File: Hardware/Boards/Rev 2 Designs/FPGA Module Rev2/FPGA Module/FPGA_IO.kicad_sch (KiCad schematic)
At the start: 55 parts, among them Q6 FDG1024NZ, Q7 FDG1024NZ, SW3 RST, U1 XCKU3P-FFVA676, U2 TXB0108DQSR, U3 Si511J200

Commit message: FPGA Module Rev 2 Layout Begun
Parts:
- removed C1, C2, C6, C7: 100nF, Capacitor_SMD:C_0201_0603Metric, symbol Device:C_Small
- removed R11, R12, R14, R15: 1K, Resistor_SMD:R_0201_0603Metric, symbol Device:R_US
- removed R13, R5: 100R, Resistor_SMD:R_0201_0603Metric, symbol Device:R_US
- removed R4: 0R, Resistor_SMD:R_0201_0603Metric, symbol Device:R_US
- removed TP10, TP9: Test Point, FPGA Module:Test Point 0.5mm No Silk, symbol Connector:TestPoint
- removed U2: TXB0108DQSR, Package_SON:USON-20_2x4mm_P0.4mm, symbol Logic_LevelTranslator:TXB0108DQSR
- added R3: 240R, Resistor_SMD:R_0201_0603Metric, symbol Device:R_US
- renumbered C44 to C1, C4 to C2, D4 to D1, D3 to D2, D2 to D3, D1 to D4, Q6 to Q1, Q7 to Q2, R16 to R10, R20 to R11, R21 to R12, R22 to R13, R23 to R14, R10 to R15, R24 to R16, R25 to R17, R26 to R18, R27 to R19, R28 to R20, R29 to R21, R30 to R22, R31 to R23, R3 to R4, R9 to R5, R8 to R6, R19 to R7, R18 to R8, R17 to R9, SW3 to SW1, TP14 to TP10, TP15 to TP11, TP16 to TP12, TP17 to TP13, TP18 to TP14, TP6 to TP5, TP7 to TP6, TP11 to TP7, TP12 to TP8, TP13 to TP9, U3 to U2
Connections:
- net FPGA_SPI_CS is gone; now on net D3_8: U1.R18 (IO_L19P_T3L_N0_DBC_AD9P_64)
- net FPGA_SPI_MISO is gone; now on net D3_11: U1.R21 (IO_L20N_T3L_N3_AD1N_64)
- net FPGA_SPI_MOSI is gone; now on net D3_10: U1.P21 (IO_L20P_T3L_N2_AD1P_64)
- net FPGA_SPI_SCK is gone; now on net D3_9: U1.T18 (IO_L19N_T3L_N1_DBC_AD9N_64)
- net HDMI_CEC is gone; now on net RST2: U1.AB22 (IO_L3N_T0L_N5_AD15N_64)
- net HDMI_CLK_SEL is gone; now on net RWDS2_0: U1.U25 (IO_T1U_N12_64)
- net HDMI_EQ_SEL is gone; now on net D2_4: U1.Y23 (IO_L5P_T0U_N8_AD14P_64)
- net HDMI_HPD_SRC is gone; now on net CK2_N: U1.AA25 (IO_L4P_T0U_N6_DBC_AD7P_64)
- net HDMI_I2C_EN is gone; now on net D2_14: U1.V24 (IO_L11N_T1U_N9_GC_64)
- net HDMI_LVCLK_N is gone; now on net IO1: U1.F8 (IO_L20N_T3L_N3_AD1N_66)
- net HDMI_LVCLK_P is gone; now on net IO6: U1.F9 (IO_L20P_T3L_N2_AD1P_66)
- net HDMI_OE is gone; now on net CS2: U1.AA22 (IO_L3P_T0L_N4_AD15P_64)
- net HDMI_SCL_SRC is gone; now on net D2_7: U1.AC24 (IO_L6N_T0U_N11_AD6N_64)
- net HDMI_SDA_SRC is gone; now on net D2_6: U1.AC23 (IO_L6P_T0U_N10_AD6P_64)
- net HDMI_SDA_SRC_EN is gone; now on net D2_3: U1.AC26 (IO_L2N_T0L_N3_64)
- net HDMI_SEL is gone; now on net D2_5: U1.AA23 (IO_L5N_T0U_N9_AD14N_64)
- net HDMI_SLEW_CTL is gone; now on net D2_2: U1.AB26 (IO_L2P_T0L_N2_64)
- net MBUS_D14 is gone; now on net FPGA_I2C_SCL: U1.AE16 (IO_L1P_AD11P_84)
- net MEMCLK_N is gone; now on net FIFO_BE0: U1.F12 (IO_L11N_T1U_N9_GC_66)
- net MEMCLK_P is gone; now on net FIFO_D0: U1.G12 (IO_L11P_T1U_N8_GC_66)
- net SYSCLK1_N is gone; now on net CK3_P: U1.T24 (IO_L13N_T2L_N1_GC_QBC_64)
- net SYSCLK1_P is gone; now on net CK3_N: U1.T23 (IO_L13P_T2L_N0_GC_QBC_64)
- net TPD5_EN is gone; now on net CK2_P: U1.AB25 (IO_L4N_T0U_N7_DBC_AD7N_64)
- net CAM_LED_EN: now also U1.AB14 (IO_L9N_AD3N_84); no longer U1.AF10 (IO_L4N_AD12N_85)
- net CAM_PWR_EN: now also U1.AA14 (IO_L9P_AD3P_84); no longer U1.AE11 (IO_L2N_AD14N_85)
- net CK2_N: no longer U1.AF22 (IO_L19N_T3L_N1_DBC_AD9N_D11_65)
- net CK2_P: no longer U1.AE22 (IO_L19P_T3L_N0_DBC_AD9P_D10_65)
- net CK3_N: no longer U1.AA20 (IO_L13N_T2L_N1_GC_QBC_A07_D23_65)
- net CK3_P: no longer U1.AA19 (IO_L13P_T2L_N0_GC_QBC_A06_D22_65)
- net CS2: no longer U1.AE26 (IO_L22N_T3U_N7_DBC_AD0N_D05_65)
- net CS3: now also U1.Y26 (IO_L9N_T1L_N5_AD12N_64); no longer U1.AE21 (IO_L16N_T2U_N7_QBC_AD3N_A01_D17_65)
- net D2_0: now also U1.AA24 (IO_L1P_T0L_N0_DBC_64); no longer U1.AD25 (IO_L24N_T3U_N11_DOUT_CSO_B_65)
- net D2_1: now also U1.AB24 (IO_L1N_T0L_N1_DBC_64); no longer U1.AD24 (IO_L24P_T3U_N10_EMCCLK_65)
- net D2_10: now also U1.W26 (IO_L8N_T1L_N3_AD5N_64); no longer U1.AC21 (IO_L17N_T2U_N9_AD10N_D15_65)
- net D2_11: now also U1.Y25 (IO_L9P_T1L_N4_AD12P_64); no longer U1.AB21 (IO_L17P_T2U_N8_AD10P_D14_65)
- net D2_12: now also U1.V26 (IO_L10N_T1U_N7_QBC_AD4N_64); no longer U1.AD19 (IO_L15N_T2L_N5_AD11N_A03_D19_65)
- net D2_13: now also U1.U24 (IO_L11P_T1U_N8_GC_64); no longer U1.AC19 (IO_L15P_T2L_N4_AD11P_A02_D18_65)
- net D2_14: no longer U1.AB20 (IO_L14N_T2L_N3_GC_A05_D21_65)
- net D2_15: now also U1.V22 (IO_L12P_T1U_N10_GC_64); no longer U1.AB19 (IO_L14P_T2L_N2_GC_A04_D20_65)
- net D2_2: no longer U1.AE23 (IO_L23N_T3U_N9_PERSTN1_I2C_SDA_65)
- net D2_3: no longer U1.AD23 (IO_L23P_T3U_N8_I2C_SCLK_65)
- net D2_4: no longer U1.AF24 (IO_L21N_T3L_N5_AD8N_D07_65)
- net D2_5: no longer U1.AF23 (IO_L21P_T3L_N4_AD8P_D06_65)
- net D2_6: no longer U1.AF25 (IO_L20N_T3L_N3_AD1N_D09_65)
- net D2_7: no longer U1.AE25 (IO_L20P_T3L_N2_AD1P_D08_65)
- net D2_8: now also U1.W24 (IO_L7N_T1L_N1_QBC_AD13N_64); no longer U1.AD21 (IO_L18N_T2U_N11_AD2N_D13_65)
- net D2_9: now also U1.W25 (IO_L8P_T1L_N2_AD5P_64); no longer U1.AD20 (IO_L18P_T2U_N10_AD2P_D12_65)
- net D3_0: now also U1.R22 (IO_L16P_T2U_N6_QBC_AD3P_64); no longer U1.AB17 (IO_L2P_T0L_N2_FOE_B_65)
- net D3_1: now also U1.R23 (IO_L16N_T2U_N7_QBC_AD3N_64); no longer U1.AC17 (IO_L2N_T0L_N3_FWE_FCS2_B_65)
- net D3_10: no longer U1.W18 (IO_L9P_T1L_N4_AD12P_A14_D30_65)
- net D3_11: no longer U1.W19 (IO_L9N_T1L_N5_AD12N_A15_D31_65)
- net D3_12: now also U1.P18 (IO_L21P_T3L_N4_AD8P_64); no longer U1.Y17 (IO_L11P_T1U_N8_GC_A10_D26_65)
- net D3_13: now also U1.P19 (IO_L21N_T3L_N5_AD8N_64); no longer U1.Y18 (IO_L11N_T1U_N9_GC_A11_D27_65)
- net D3_14: now also U1.T22 (IO_L14P_T2L_N2_GC_64); no longer U1.Y20 (IO_L12N_T1U_N11_GC_A09_D25_65)
- net D3_15: now also U1.U22 (IO_L14N_T2L_N3_GC_64); no longer U1.W20 (IO_L12P_T1U_N10_GC_A08_D24_65)
- net D3_2: now also U1.P23 (IO_L17P_T2U_N8_AD10P_64); no longer U1.AE17 (IO_L3P_T0L_N4_AD15P_A26_65)
- net D3_3: now also U1.P24 (IO_L17N_T2U_N9_AD10N_64); no longer U1.AE18 (IO_L3N_T0L_N5_AD15N_A27_65)
- net D3_4: now also U1.P25 (IO_L18P_T2U_N10_AD2P_64); no longer U1.AC18 (IO_L5P_T0U_N8_AD14P_A22_65)
- net D3_5: now also U1.R25 (IO_L18N_T2U_N11_AD2N_64); no longer U1.AD18 (IO_L5N_T0U_N9_AD14N_A23_65)
- net D3_6: now also U1.T25 (IO_T2U_N12_64); no longer U1.AF17 (IO_L6P_T0U_N10_AD6P_A20_65)
- net D3_7: now also U1.V21 (IO_T3U_N12_64); no longer U1.AF18 (IO_L6N_T0U_N11_AD6N_A21_65)
- net D3_8: no longer U1.W21 (IO_L8P_T1L_N2_AD5P_A16_65)
- net D3_9: no longer U1.Y21 (IO_L8N_T1L_N3_AD5N_A17_65)
- net FIFO_BE0: no longer U1.W13 (IO_L10N_AD2N_84)
- net FIFO_BE1: now also U1.E13 (IO_L12P_T1U_N10_GC_66); no longer U1.AA14 (IO_L9P_AD3P_84)
- net FIFO_CLK: now also U1.E10 (IO_L13P_T2L_N0_GC_QBC_66); no longer U1.AA15 (IO_L7P_HDGC_AD5P_84)
- net FIFO_D0: no longer U1.W9 (IO_L11P_AD9P_85)
- net FIFO_D1: now also U1.F13 (IO_L10N_T1U_N7_QBC_AD4N_66); no longer U1.AA9 (IO_L7N_HDGC_85)
- net FIFO_D10: now also U1.D15 (IO_T0U_N12_VRP_66); no longer U1.V11 (IO_L10N_AD10N_85)
- net FIFO_D11: now also U1.A12 (IO_L6N_T0U_N11_AD6N_66); no longer U1.Y11 (IO_L8P_HDGC_85)
- net FIFO_D12: now also U1.A13 (IO_L6P_T0U_N10_AD6P_66); no longer U1.AA10 (IO_L7P_HDGC_85)
- net FIFO_D13: now also U1.B12 (IO_L5N_T0U_N9_AD14N_66); no longer U1.AB10 (IO_L6P_HDGC_85)
- net FIFO_D14: now also U1.C12 (IO_L5P_T0U_N8_AD14P_66); no longer U1.W15 (IO_L8P_HDGC_AD4P_84)
- net FIFO_D15: now also U1.A14 (IO_L4N_T0U_N7_DBC_AD7N_66); no longer U1.Y15 (IO_L8N_HDGC_AD4N_84)
- net FIFO_D2: now also U1.F14 (IO_L10P_T1U_N6_QBC_AD4P_66); no longer U1.Y10 (IO_L8N_HDGC_85)
- net FIFO_D3: now also U1.H13 (IO_L9N_T1L_N5_AD12N_66); no longer U1.W11 (IO_L12P_AD8P_85)
- net FIFO_D4: now also U1.J13 (IO_L9P_T1L_N4_AD12P_66); no longer U1.V12 (IO_L10P_AD10P_85)
- net FIFO_D5: now also U1.F15 (IO_L8N_T1L_N3_AD5N_66); no longer U1.AB9 (IO_L6N_HDGC_85)
- net FIFO_D6: now also U1.G15 (IO_L8P_T1L_N2_AD5P_66); no longer U1.AC12 (IO_L1P_AD15P_85)
- net FIFO_D7: now also U1.G14 (IO_L7N_T1L_N1_QBC_AD13N_66); no longer U1.W14 (IO_L10P_AD2P_84)
- net FIFO_D8: now also U1.H14 (IO_L7P_T1L_N0_QBC_AD13P_66); no longer U1.AA8 (IO_L9N_AD11N_85)
- net FIFO_D9: now also U1.E15 (IO_T1U_N12_66); no longer U1.W10 (IO_L12N_AD8N_85)
- net FPGA_I2C_SCL: no longer U1.AC11 (IO_L1N_AD15N_85)
- net FPGA_I2C_SDA: now also U1.AF15 (IO_L1N_AD11N_84); no longer U1.AD11 (IO_L2P_AD14P_85)
- net FT600_OE: now also U1.B15 (IO_L2P_T0L_N2_66); no longer U1.AC9 (IO_L3P_AD13P_85)
- net FT600_RD: now also U1.A15 (IO_L2N_T0L_N3_66); no longer U1.Y8 (IO_L9P_AD11P_85)
- net FT600_RST: now also U1.C14 (IO_L1N_T0L_N1_DBC_66); no longer U1.AD8 (IO_L5N_HDGC_85)
- net FT600_RXE: now also U1.C13 (IO_L3N_T0L_N5_AD15N_66); no longer U1.AD9 (IO_L3N_AD13N_85)
- net FT600_TXE: now also U1.B14 (IO_L4P_T0U_N6_DBC_AD7P_66); no longer U1.AE10 (IO_L4P_AD12P_85)
- net FT600_WAKEUP: now also U1.D14 (IO_L1P_T0L_N0_DBC_66); no longer U1.AC8 (IO_L5P_HDGC_85)
- net FT600_WR: now also U1.D13 (IO_L3P_T0L_N4_AD15P_66); no longer U1.W8 (IO_L11N_AD9N_85)
- net GND: now also U1.A3 (MGTYRXN3_227), U1.A4 (MGTYRXP3_227), U1.AB1 (MGTYRXN3_224), U1.AB2 (MGTYRXP3_224), U1.AD1 (MGTYRXN2_224), U1.AD2 (MGTYRXP2_224), U1.AE3 (MGTYRXN1_224), U1.AE4 (MGTYRXP1_224), U1.AF1 (MGTYRXN0_224), U1.AF2 (MGTYRXP0_224), U1.AF7 (MGTRREF_R), U1.AF8 (MGTAVTTRCAL_R)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
- net IO0: now also U1.J9 (IO_L21N_T3L_N5_AD8N_66); no longer U1.P23 (IO_L17P_T2U_N8_AD10P_64)
- net IO1: no longer U1.P25 (IO_L18P_T2U_N10_AD2P_64)
- net IO2: now also U1.H9 (IO_L19P_T3L_N0_DBC_AD9P_66); no longer U1.V21 (IO_T3U_N12_64)
- net IO3: now also U1.H8 (IO_L19N_T3L_N1_DBC_AD9N_66); no longer U1.T25 (IO_T2U_N12_64)
- net IO4: now also U1.G11 (IO_L22P_T3U_N6_DBC_AD0P_66); no longer U1.R23 (IO_L16N_T2U_N7_QBC_AD3N_64)
- net IO5: now also U1.F10 (IO_L22N_T3U_N7_DBC_AD0N_66); no longer U1.R22 (IO_L16P_T2U_N6_QBC_AD3P_64)
- net IO6: no longer U1.R25 (IO_L18N_T2U_N11_AD2N_64)
- net IO7: now also U1.J10 (IO_L21P_T3L_N4_AD8P_66); no longer U1.P24 (IO_L17N_T2U_N9_AD10N_64)
- net LED0: now also U1.J11 (IO_L23P_T3U_N8_66); no longer U1.V26 (IO_L10N_T1U_N7_QBC_AD4N_64)
- net LED1: now also U1.H11 (IO_L23N_T3U_N9_66); no longer U1.U26 (IO_L10P_T1U_N6_QBC_AD4P_64)
- net LED2: now also U1.G10 (IO_L24P_T3U_N10_66); no longer U1.Y26 (IO_L9N_T1L_N5_AD12N_64)
- net LED3: now also U1.G9 (IO_L24N_T3U_N11_66); no longer U1.W26 (IO_L8N_T1L_N3_AD5N_64)
- net MBUS_D0: now also U1.E11 (IO_L14P_T2L_N2_GC_66); no longer U1.AD13 (IO_L6N_HDGC_AD6N_84)
- net MBUS_D1: now also U1.D11 (IO_L14N_T2L_N3_GC_66); no longer U1.AD14 (IO_L6P_HDGC_AD6P_84)
- net MBUS_D10: now also U1.D9 (IO_T2U_N12_66); no longer U1.AF14 (IO_L2P_AD10P_84)
- net MBUS_D11: now also U1.H12 (IO_T3U_N12_66); no longer U1.AF15 (IO_L1N_AD11N_84)
- net MBUS_D2: now also U1.C9 (IO_L15P_T2L_N4_AD11P_66); no longer U1.AD15 (IO_L3P_AD9P_84)
- net MBUS_D3: now also U1.C8 (IO_L15N_T2L_N5_AD11N_66); no longer U1.AC13 (IO_L5N_HDGC_AD7N_84)
- net MBUS_D4: now also U1.C11 (IO_L16P_T2U_N6_QBC_AD3P_66); no longer U1.AC14 (IO_L5P_HDGC_AD7P_84)
- net MBUS_D5: now also U1.B11 (IO_L16N_T2U_N7_QBC_AD3N_66); no longer U1.AB14 (IO_L9N_AD3N_84)
- net MBUS_D6: now also U1.E8 (IO_L17P_T2U_N8_AD10P_66); no longer U1.AB15 (IO_L7N_HDGC_AD5N_84)
- net MBUS_D7: now also U1.D8 (IO_L17N_T2U_N9_AD10N_66); no longer U1.AA13 (IO_L11P_AD1P_84)
- net MBUS_D8: now also U1.B10 (IO_L18P_T2U_N10_AD2P_66); no longer U1.AF12 (IO_L4N_AD8N_84)
- net MBUS_D9: now also U1.A10 (IO_L18N_T2U_N11_AD2N_66); no longer U1.AF13 (IO_L2N_AD10N_84)
- net MIPI_CLK_N: now also U1.AA20 (IO_L13N_T2L_N1_GC_QBC_A07_D23_65); no longer U1.D10 (IO_L13N_T2L_N1_GC_QBC_66)
- net MIPI_CLK_P: now also U1.AA19 (IO_L13P_T2L_N0_GC_QBC_A06_D22_65); no longer U1.E10 (IO_L13P_T2L_N0_GC_QBC_66)
- net MIPI_D0_N: now also U1.AB20 (IO_L14N_T2L_N3_GC_A05_D21_65); no longer U1.D11 (IO_L14N_T2L_N3_GC_66)
- net MIPI_D0_P: now also U1.AB19 (IO_L14P_T2L_N2_GC_A04_D20_65); no longer U1.E11 (IO_L14P_T2L_N2_GC_66)
- net MIPI_D1_N: now also U1.AD19 (IO_L15N_T2L_N5_AD11N_A03_D19_65); no longer U1.C8 (IO_L15N_T2L_N5_AD11N_66)
- net MIPI_D1_P: now also U1.AC19 (IO_L15P_T2L_N4_AD11P_A02_D18_65); no longer U1.C9 (IO_L15P_T2L_N4_AD11P_66)
- net MIPI_D2_N: now also U1.AD21 (IO_L18N_T2U_N11_AD2N_D13_65); no longer U1.A10 (IO_L18N_T2U_N11_AD2N_66)
- net MIPI_D2_P: now also U1.AD20 (IO_L18P_T2U_N10_AD2P_D12_65); no longer U1.B10 (IO_L18P_T2U_N10_AD2P_66)
- net MIPI_D3_N: now also U1.AC21 (IO_L17N_T2U_N9_AD10N_D15_65); no longer U1.D8 (IO_L17N_T2U_N9_AD10N_66)
- net MIPI_D3_P: now also U1.AB21 (IO_L17P_T2U_N8_AD10P_D14_65); no longer U1.E8 (IO_L17P_T2U_N8_AD10P_66)
- net RST2: no longer U1.AD26 (IO_L22P_T3U_N6_DBC_AD0P_D04_65)
- net RST3: now also U1.U26 (IO_L10P_T1U_N6_QBC_AD4P_64); no longer U1.AE20 (IO_L16P_T2U_N6_QBC_AD3P_A00_D16_65)
- net RWDS2_0: no longer U1.AC22 (IO_T3U_N12_PERSTN0_65)
- net RWDS2_1: now also U1.W23 (IO_L7P_T1L_N0_QBC_AD13P_64); no longer U1.AA18 (IO_T2U_N12_CSI_ADV_B_65)
- net RWDS3_0: now also U1.P26 (IO_L15P_T2L_N4_AD11P_64); no longer U1.AC16 (IO_L1P_T0L_N0_DBC_RS0_65)
- net RWDS3_1: now also U1.R26 (IO_L15N_T2L_N5_AD11N_64); no longer U1.AD16 (IO_L1N_T0L_N1_DBC_RS1_65)
- net SYS_SPI_CS: now also U1.W13 (IO_L10N_AD2N_84)
- net SYS_SPI_MISO: now also U1.W14 (IO_L10P_AD2P_84)
- net SYS_SPI_MOSI: now also U1.AA12 (IO_L11N_AD1N_84)
- net SYS_SPI_SCK: now also U1.AA13 (IO_L11P_AD1P_84)
- net UART_RX: now also U1.AB11 (IO_L12N_AD0N_84); no longer U1.P26 (IO_L15P_T2L_N4_AD11P_64)
- net UART_TX: now also U1.AB12 (IO_L12P_AD0P_84); no longer U1.R26 (IO_L15N_T2L_N5_AD11N_64)
- net at R15.2: now also U1.AF18 (IO_L6N_T0U_N11_AD6N_A21_65); no longer U1.D15 (IO_T0U_N12_VRP_66)
- net GTCLK0_N: no longer names the net of U1.M5 (MGTREFCLK0N_226)
- net GTCLK0_P: no longer names the net of U1.M6 (MGTREFCLK0P_226)
- net GTCLK1_N: no longer names the net of U1.K5 (MGTREFCLK1N_226)
- net GTCLK1_P: no longer names the net of U1.K6 (MGTREFCLK1P_226)
- net HDMI_D0_N: no longer names the net of U1.J3 (MGTYTXN2_226)
- net HDMI_D0_P: no longer names the net of U1.J4 (MGTYTXP2_226)
- net HDMI_D1_N: no longer names the net of U1.L3 (MGTYTXN1_226)
- net HDMI_D1_P: no longer names the net of U1.L4 (MGTYTXP1_226)
- net HDMI_D2_N: no longer names the net of U1.N3 (MGTYTXN0_226)
- net HDMI_D2_P: no longer names the net of U1.N4 (MGTYTXP0_226)
- net HDMI_GTCLK_N: no longer names the net of U1.G3 (MGTYTXN3_226)
- net HDMI_GTCLK_P: no longer names the net of U1.G4 (MGTYTXP3_226)
- net HDMI_PRE_SEL: no longer names the net of U1.Y22 (IO_T0U_N12_VRP_64)
- net HDMI_PRE_SEL: now also R3.2
- net MBUS_D12 renamed HDMI_SD0_DL0
- net MBUS_D13 renamed HDMI_SD1_DR1
- new net HDMI_DB0: U1.Y8 (IO_L9P_AD11P_85)
- new net HDMI_DB1: U1.AA8 (IO_L9N_AD11N_85)
- new net HDMI_DB2: U1.V12 (IO_L10P_AD10P_85)
- new net HDMI_DB3: U1.V11 (IO_L10N_AD10N_85)
- new net HDMI_DB4: U1.W9 (IO_L11P_AD9P_85)
- new net HDMI_DB5: U1.W8 (IO_L11N_AD9N_85)
- new net HDMI_DB6: U1.W11 (IO_L12P_AD8P_85)
- new net HDMI_DB7: U1.W10 (IO_L12N_AD8N_85)
- new net HDMI_DE: U1.Y15 (IO_L8N_HDGC_AD4N_84)
- new net HDMI_DG0: U1.AC8 (IO_L5P_HDGC_85)
- new net HDMI_DG1: U1.AD8 (IO_L5N_HDGC_85)
- new net HDMI_DG2: U1.AB10 (IO_L6P_HDGC_85)
- new net HDMI_DG3: U1.AB9 (IO_L6N_HDGC_85)
- new net HDMI_DG4: U1.AA10 (IO_L7P_HDGC_85)
- new net HDMI_DG5: U1.AA9 (IO_L7N_HDGC_85)
- new net HDMI_DG6: U1.Y11 (IO_L8P_HDGC_85)
- new net HDMI_DG7: U1.Y10 (IO_L8N_HDGC_85)
- new net HDMI_DR0: U1.AC12 (IO_L1P_AD15P_85)
- new net HDMI_DR1: U1.AC11 (IO_L1N_AD15N_85)
- new net HDMI_DR2: U1.AD11 (IO_L2P_AD14P_85)
- new net HDMI_DR3: U1.AE11 (IO_L2N_AD14N_85)
- new net HDMI_DR4: U1.AC9 (IO_L3P_AD13P_85)
- new net HDMI_DR5: U1.AD9 (IO_L3N_AD13N_85)
- new net HDMI_DR6: U1.AE10 (IO_L4P_AD12P_85)
- new net HDMI_DR7: U1.AF10 (IO_L4N_AD12N_85)
- new net HDMI_HSYNC: U1.W15 (IO_L8P_HDGC_AD4P_84)
- new net HDMI_IDCLK: U1.AA15 (IO_L7P_HDGC_AD5P_84)
- new net HDMI_INT: U1.AD14 (IO_L6P_HDGC_AD6P_84)
- new net HDMI_MCLK: U1.AC13 (IO_L5N_HDGC_AD7N_84)
- new net HDMI_RST: U1.AD13 (IO_L6N_HDGC_AD6N_84)
- new net HDMI_SCK: U1.AC14 (IO_L5P_HDGC_AD7P_84)
- new net HDMI_SD2_DL1: U1.AD15 (IO_L3P_AD9P_84)
- new net HDMI_SD3_DR2: U1.AF13 (IO_L2N_AD10N_84)
- new net HDMI_SPDIF: U1.AF14 (IO_L2P_AD10P_84)
- new net HDMI_VSYNC: U1.AB15 (IO_L7N_HDGC_AD5N_84)
- new net HDMI_WS_DR0: U1.AF12 (IO_L4N_AD8N_84)
- no-connect marks 113 -> 101
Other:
- note removed: "HDMI"
- moved on the sheet: D1, D2, D3, D4, Q1A, Q1B, Q2A, Q2B, R10, R11, R12, R13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

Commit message: Completed B2B and HyperRam routing
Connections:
- net CK0_N: now also U1.A25 (IO_L1N_T0L_N1_DBC_67); no longer U1.A18 (IO_L15N_T2L_N5_AD11N_67)
- net CK0_P: now also U1.A24 (IO_L1P_T0L_N0_DBC_67); no longer U1.A17 (IO_L15P_T2L_N4_AD11P_67)
- net CK1_N: now also U1.C18 (IO_L14N_T2L_N3_GC_67); no longer U1.A23 (IO_L7N_T1L_N1_QBC_AD13N_67)
- net CK1_P: now also U1.D18 (IO_L14P_T2L_N2_GC_67); no longer U1.A22 (IO_L7P_T1L_N0_QBC_AD13P_67)
- net CK2_N: now also U1.P24 (IO_L17N_T2U_N9_AD10N_64); no longer U1.AA25 (IO_L4P_T0U_N6_DBC_AD7P_64)
- net CK2_P: now also U1.P23 (IO_L17P_T2U_N8_AD10P_64); no longer U1.AB25 (IO_L4N_T0U_N7_DBC_AD7N_64)
- net CK3_N: now also U1.V26 (IO_L10N_T1U_N7_QBC_AD4N_64); no longer U1.T23 (IO_L13P_T2L_N0_GC_QBC_64)
- net CK3_P: now also U1.U26 (IO_L10P_T1U_N6_QBC_AD4P_64); no longer U1.T24 (IO_L13N_T2L_N1_GC_QBC_64)
- net CS0: now also U1.A23 (IO_L7N_T1L_N1_QBC_AD13N_67); no longer U1.B17 (IO_L18N_T2U_N11_AD2N_67)
- net CS1: now also U1.C17 (IO_L18P_T2U_N10_AD2P_67); no longer U1.A20 (IO_L8N_T1L_N3_AD5N_67)
- net CS2: now also U1.R22 (IO_L16P_T2U_N6_QBC_AD3P_64); no longer U1.AA22 (IO_L3P_T0L_N4_AD15P_64)
- net CS3: now also U1.U25 (IO_T1U_N12_64); no longer U1.Y26 (IO_L9N_T1L_N5_AD12N_64)
- net D0_0: now also U1.B21 (IO_L9P_T1L_N4_AD12P_67); no longer U1.E17 (IO_L23P_T3U_N8_67)
- net D0_1: now also U1.C21 (IO_L10P_T1U_N6_QBC_AD4P_67); no longer U1.G17 (IO_L20P_T3L_N2_AD1P_67)
- net D0_10: now also U1.B26 (IO_L6N_T0U_N11_AD6N_67); no longer U1.F20 (IO_L19N_T3L_N1_DBC_AD9N_67)
- net D0_11: now also U1.C22 (IO_L10N_T1U_N7_QBC_AD4N_67); no longer U1.C16 (IO_L17P_T2U_N8_AD10P_67)
- net D0_12: now also U1.D25 (IO_L2P_T0L_N2_67); no longer U1.D19 (IO_L13P_T2L_N0_GC_QBC_67)
- net D0_13: now also U1.C23 (IO_L4N_T0U_N7_DBC_AD7N_67); no longer U1.B19 (IO_L16P_T2U_N6_QBC_AD3P_67)
- net D0_14: now also U1.D26 (IO_L2N_T0L_N3_67); no longer U1.F19 (IO_L21N_T3L_N5_AD8N_67)
- net D0_15: now also U1.C24 (IO_L5N_T0U_N9_AD14N_67); no longer U1.A19 (IO_L16N_T2U_N7_QBC_AD3N_67)
- net D0_2: now also U1.A20 (IO_L8N_T1L_N3_AD5N_67); no longer U1.G19 (IO_L19P_T3L_N0_DBC_AD9P_67)
- net D0_3: now also U1.B25 (IO_L3N_T0L_N5_AD15N_67); no longer U1.F18 (IO_L21P_T3L_N4_AD8P_67)
- net D0_4: now also U1.A19 (IO_L16N_T2U_N7_QBC_AD3N_67); no longer U1.B16 (IO_L17N_T2U_N9_AD10N_67)
- net D0_5: now also U1.B24 (IO_L3P_T0L_N4_AD15P_67); no longer U1.E18 (IO_L23N_T3U_N9_67)
- net D0_6: now also U1.D23 (IO_L4P_T0U_N6_DBC_AD7P_67); no longer U1.E16 (IO_T3U_N12_67)
- net D0_7: now also U1.D21 (IO_L12N_T1U_N11_GC_67); no longer U1.D16 (IO_T2U_N12_67)
- net D0_8: now also U1.D24 (IO_L5P_T0U_N8_AD14P_67); no longer U1.D18 (IO_L14P_T2L_N2_GC_67)
- net D0_9: now also U1.B22 (IO_L9N_T1L_N5_AD12N_67); no longer U1.C18 (IO_L14N_T2L_N3_GC_67)
- net D1_0: now also U1.D20 (IO_L12P_T1U_N10_GC_67); no longer U1.B21 (IO_L9P_T1L_N4_AD12P_67)
- net D1_1: now also U1.E21 (IO_L11N_T1U_N9_GC_67); no longer U1.B22 (IO_L9N_T1L_N5_AD12N_67)
- net D1_10: now also U1.H18 (IO_L24N_T3U_N11_67); no longer U1.D26 (IO_L2N_T0L_N3_67)
- net D1_11: now also U1.E17 (IO_L23P_T3U_N8_67); no longer U1.E21 (IO_L11N_T1U_N9_GC_67)
- net D1_12: now also U1.G17 (IO_L20P_T3L_N2_AD1P_67); no longer U1.C26 (IO_L6P_T0U_N10_AD6P_67)
- net D1_13: now also U1.E16 (IO_T3U_N12_67); no longer U1.A24 (IO_L1P_T0L_N0_DBC_67)
- net D1_14: now also U1.G19 (IO_L19P_T3L_N0_DBC_AD9P_67); no longer U1.C24 (IO_L5N_T0U_N9_AD14N_67)
- net D1_15: now also U1.E18 (IO_L23N_T3U_N9_67); no longer U1.A25 (IO_L1N_T0L_N1_DBC_67)
- net D1_2: now also U1.A17 (IO_L15P_T2L_N4_AD11P_67); no longer U1.D25 (IO_L2P_T0L_N2_67)
- net D1_3: now also U1.F19 (IO_L21N_T3L_N5_AD8N_67); no longer U1.C21 (IO_L10P_T1U_N6_QBC_AD4P_67)
- net D1_4: now also U1.A18 (IO_L15N_T2L_N5_AD11N_67); no longer U1.D24 (IO_L5P_T0U_N8_AD14P_67)
- net D1_5: now also U1.F20 (IO_L19N_T3L_N1_DBC_AD9N_67); no longer U1.C23 (IO_L4N_T0U_N7_DBC_AD7N_67)
- net D1_6: now also U1.E20 (IO_L11P_T1U_N8_GC_67); no longer U1.C22 (IO_L10N_T1U_N7_QBC_AD4N_67)
- net D1_7: now also U1.C16 (IO_L17P_T2U_N8_AD10P_67); no longer U1.E20 (IO_L11P_T1U_N8_GC_67)
- net D1_8: now also U1.F17 (IO_L20N_T3L_N3_AD1N_67); no longer U1.B25 (IO_L3N_T0L_N5_AD15N_67)
- net D1_9: now also U1.D16 (IO_T2U_N12_67); no longer U1.B24 (IO_L3P_T0L_N4_AD15P_67)
- net D2_0: now also U1.T20 (IO_L22N_T3U_N7_DBC_AD0N_64); no longer U1.AA24 (IO_L1P_T0L_N0_DBC_64)
- net D2_1: now also U1.R20 (IO_L23N_T3U_N9_64); no longer U1.AB24 (IO_L1N_T0L_N1_DBC_64)
- net D2_10: now also U1.V23 (IO_L12N_T1U_N11_GC_64); no longer U1.W26 (IO_L8N_T1L_N3_AD5N_64)
- net D2_11: now also U1.U21 (IO_L24N_T3U_N11_64); no longer U1.Y25 (IO_L9P_T1L_N4_AD12P_64)
- net D2_12: now also U1.V22 (IO_L12P_T1U_N10_GC_64); no longer U1.V26 (IO_L10N_T1U_N7_QBC_AD4N_64)
- net D2_13: now also U1.U22 (IO_L14N_T2L_N3_GC_64); no longer U1.U24 (IO_L11P_T1U_N8_GC_64)
- net D2_15: now also U1.R26 (IO_L15N_T2L_N5_AD11N_64); no longer U1.V22 (IO_L12P_T1U_N10_GC_64)
- net D2_2: now also U1.R21 (IO_L20N_T3L_N3_AD1N_64); no longer U1.AB26 (IO_L2P_T0L_N2_64)
- net D2_3: now also U1.P21 (IO_L20P_T3L_N2_AD1P_64); no longer U1.AC26 (IO_L2N_T0L_N3_64)
- net D2_4: now also U1.P20 (IO_L23P_T3U_N8_64); no longer U1.Y23 (IO_L5P_T0U_N8_AD14P_64)
- net D2_5: now also U1.V21 (IO_T3U_N12_64); no longer U1.AA23 (IO_L5N_T0U_N9_AD14N_64)
- net D2_6: now also U1.U20 (IO_L24P_T3U_N10_64); no longer U1.AC23 (IO_L6P_T0U_N10_AD6P_64)
- net D2_7: now also U1.T19 (IO_L22P_T3U_N6_DBC_AD0P_64); no longer U1.AC24 (IO_L6N_T0U_N11_AD6N_64)
- net D2_8: now also U1.T25 (IO_T2U_N12_64); no longer U1.W24 (IO_L7N_T1L_N1_QBC_AD13N_64)
- net D2_9: now also U1.T23 (IO_L13P_T2L_N0_GC_QBC_64); no longer U1.W25 (IO_L8P_T1L_N2_AD5P_64)
- net D3_0: now also U1.Y25 (IO_L9P_T1L_N4_AD12P_64); no longer U1.R22 (IO_L16P_T2U_N6_QBC_AD3P_64)
- net D3_1: now also U1.Y26 (IO_L9N_T1L_N5_AD12N_64); no longer U1.R23 (IO_L16N_T2U_N7_QBC_AD3N_64)
- net D3_10: now also U1.AC26 (IO_L2N_T0L_N3_64); no longer U1.P21 (IO_L20P_T3L_N2_AD1P_64)
- net D3_11: now also U1.AA24 (IO_L1P_T0L_N0_DBC_64); no longer U1.R21 (IO_L20N_T3L_N3_AD1N_64)
- net D3_12: now also U1.AC24 (IO_L6N_T0U_N11_AD6N_64); no longer U1.P18 (IO_L21P_T3L_N4_AD8P_64)
- net D3_13: now also U1.AA22 (IO_L3P_T0L_N4_AD15P_64); no longer U1.P19 (IO_L21N_T3L_N5_AD8N_64)
- net D3_14: now also U1.AB25 (IO_L4N_T0U_N7_DBC_AD7N_64); no longer U1.T22 (IO_L14P_T2L_N2_GC_64)
- net D3_15: now also U1.AB22 (IO_L3N_T0L_N5_AD15N_64); no longer U1.U22 (IO_L14N_T2L_N3_GC_64)
- net D3_2: now also U1.W26 (IO_L8N_T1L_N3_AD5N_64); no longer U1.P23 (IO_L17P_T2U_N8_AD10P_64)
- net D3_3: now also U1.W25 (IO_L8P_T1L_N2_AD5P_64); no longer U1.P24 (IO_L17N_T2U_N9_AD10N_64)
- net D3_4: now also U1.W24 (IO_L7N_T1L_N1_QBC_AD13N_64); no longer U1.P25 (IO_L18P_T2U_N10_AD2P_64)
- net D3_5: now also U1.AB26 (IO_L2P_T0L_N2_64); no longer U1.R25 (IO_L18N_T2U_N11_AD2N_64)
- net D3_6: now also U1.AA25 (IO_L4P_T0U_N6_DBC_AD7P_64); no longer U1.T25 (IO_T2U_N12_64)
- net D3_7: now also U1.AA23 (IO_L5N_T0U_N9_AD14N_64); no longer U1.V21 (IO_T3U_N12_64)
- net D3_8: now also U1.AB24 (IO_L1N_T0L_N1_DBC_64); no longer U1.R18 (IO_L19P_T3L_N0_DBC_AD9P_64)
- net D3_9: now also U1.W23 (IO_L7P_T1L_N0_QBC_AD13P_64); no longer U1.T18 (IO_L19N_T3L_N1_DBC_AD9N_64)
- net FIFO_BE0: now also U1.E11 (IO_L14P_T2L_N2_GC_66); no longer U1.F12 (IO_L11N_T1U_N9_GC_66)
- net FIFO_BE1: now also U1.F12 (IO_L11N_T1U_N9_GC_66); no longer U1.E13 (IO_L12P_T1U_N10_GC_66)
- net FIFO_CLK: now also U1.E13 (IO_L12P_T1U_N10_GC_66); no longer U1.E10 (IO_L13P_T2L_N0_GC_QBC_66)
- net FIFO_D0: now also U1.E15 (IO_T1U_N12_66); no longer U1.G12 (IO_L11P_T1U_N8_GC_66)
- net FIFO_D1: now also U1.D15 (IO_T0U_N12_VRP_66); no longer U1.F13 (IO_L10N_T1U_N7_QBC_AD4N_66)
- net FIFO_D10: now also U1.A12 (IO_L6N_T0U_N11_AD6N_66); no longer U1.D15 (IO_T0U_N12_VRP_66)
- net FIFO_D11: now also U1.B12 (IO_L5N_T0U_N9_AD14N_66); no longer U1.A12 (IO_L6N_T0U_N11_AD6N_66)
- net FIFO_D12: now also U1.E8 (IO_L17P_T2U_N8_AD10P_66); no longer U1.A13 (IO_L6P_T0U_N10_AD6P_66)
- net FIFO_D13: now also U1.D8 (IO_L17N_T2U_N9_AD10N_66); no longer U1.B12 (IO_L5N_T0U_N9_AD14N_66)
- net FIFO_D14: now also U1.C8 (IO_L15N_T2L_N5_AD11N_66); no longer U1.C12 (IO_L5P_T0U_N8_AD14P_66)
- net FIFO_D15: now also U1.D9 (IO_T2U_N12_66); no longer U1.A14 (IO_L4N_T0U_N7_DBC_AD7N_66)
- net FIFO_D2: now also U1.A15 (IO_L2N_T0L_N3_66); no longer U1.F14 (IO_L10P_T1U_N6_QBC_AD4P_66)
- net FIFO_D3: now also U1.B15 (IO_L2P_T0L_N2_66); no longer U1.H13 (IO_L9N_T1L_N5_AD12N_66)
- net FIFO_D4: now also U1.B14 (IO_L4P_T0U_N6_DBC_AD7P_66); no longer U1.J13 (IO_L9P_T1L_N4_AD12P_66)
- net FIFO_D5: now also U1.A14 (IO_L4N_T0U_N7_DBC_AD7N_66); no longer U1.F15 (IO_L8N_T1L_N3_AD5N_66)
- net FIFO_D6: now also U1.D13 (IO_L3P_T0L_N4_AD15P_66); no longer U1.G15 (IO_L8P_T1L_N2_AD5P_66)
- net FIFO_D7: now also U1.C13 (IO_L3N_T0L_N5_AD15N_66); no longer U1.G14 (IO_L7N_T1L_N1_QBC_AD13N_66)
- net FIFO_D8: now also U1.F13 (IO_L10N_T1U_N7_QBC_AD4N_66); no longer U1.H14 (IO_L7P_T1L_N0_QBC_AD13P_66)
- net FIFO_D9: now also U1.C12 (IO_L5P_T0U_N8_AD14P_66); no longer U1.E15 (IO_T1U_N12_66)
- net FPGA_I2C_SCL: now also U1.AF15 (IO_L1N_AD11N_84); no longer U1.AE16 (IO_L1P_AD11P_84)
- net FPGA_I2C_SDA: now also U1.AE16 (IO_L1P_AD11P_84); no longer U1.AF15 (IO_L1N_AD11N_84)
- net FT600_OE: now also U1.B10 (IO_L18P_T2U_N10_AD2P_66); no longer U1.B15 (IO_L2P_T0L_N2_66)
- net FT600_RD: now also U1.A10 (IO_L18N_T2U_N11_AD2N_66); no longer U1.A15 (IO_L2N_T0L_N3_66)
- net FT600_RST: now also U1.E10 (IO_L13P_T2L_N0_GC_QBC_66); no longer U1.C14 (IO_L1N_T0L_N1_DBC_66)
- net FT600_RXE: now also U1.C11 (IO_L16P_T2U_N6_QBC_AD3P_66); no longer U1.C13 (IO_L3N_T0L_N5_AD15N_66)
- net FT600_TXE: now also U1.B11 (IO_L16N_T2U_N7_QBC_AD3N_66); no longer U1.B14 (IO_L4P_T0U_N6_DBC_AD7P_66)
- net FT600_WAKEUP: now also U1.C9 (IO_L15P_T2L_N4_AD11P_66); no longer U1.D14 (IO_L1P_T0L_N0_DBC_66)
- net FT600_WR: now also U1.D11 (IO_L14N_T2L_N3_GC_66); no longer U1.D13 (IO_L3P_T0L_N4_AD15P_66)
- net HDMI_DB0: now also U1.AC12 (IO_L1P_AD15P_85); no longer U1.Y8 (IO_L9P_AD11P_85)
- net HDMI_DB1: now also U1.AC11 (IO_L1N_AD15N_85); no longer U1.AA8 (IO_L9N_AD11N_85)
- net HDMI_DB2: now also U1.AD11 (IO_L2P_AD14P_85); no longer U1.V12 (IO_L10P_AD10P_85)
- net HDMI_DB3: now also U1.AE11 (IO_L2N_AD14N_85); no longer U1.V11 (IO_L10N_AD10N_85)
- net HDMI_DB4: now also U1.AE10 (IO_L4P_AD12P_85); no longer U1.W9 (IO_L11P_AD9P_85)
- net HDMI_DB5: now also U1.AF10 (IO_L4N_AD12N_85); no longer U1.W8 (IO_L11N_AD9N_85)
- net HDMI_DB6: now also U1.AC9 (IO_L3P_AD13P_85); no longer U1.W11 (IO_L12P_AD8P_85)
- net HDMI_DB7: now also U1.AD9 (IO_L3N_AD13N_85); no longer U1.W10 (IO_L12N_AD8N_85)
- net HDMI_DE: now also U1.AA15 (IO_L7P_HDGC_AD5P_84); no longer U1.Y15 (IO_L8N_HDGC_AD4N_84)
- net HDMI_DG0: now also U1.Y11 (IO_L8P_HDGC_85); no longer U1.AC8 (IO_L5P_HDGC_85)
- net HDMI_DG1: now also U1.Y10 (IO_L8N_HDGC_85); no longer U1.AD8 (IO_L5N_HDGC_85)
- net HDMI_DG2: now also U1.AA10 (IO_L7P_HDGC_85); no longer U1.AB10 (IO_L6P_HDGC_85)
- net HDMI_DG3: now also U1.AB10 (IO_L6P_HDGC_85); no longer U1.AB9 (IO_L6N_HDGC_85)
- net HDMI_DG4: now also U1.AA9 (IO_L7N_HDGC_85); no longer U1.AA10 (IO_L7P_HDGC_85)
- net HDMI_DG5: now also U1.AB9 (IO_L6N_HDGC_85); no longer U1.AA9 (IO_L7N_HDGC_85)
- net HDMI_DG6: now also U1.AC8 (IO_L5P_HDGC_85); no longer U1.Y11 (IO_L8P_HDGC_85)
- net HDMI_DG7: now also U1.AD8 (IO_L5N_HDGC_85); no longer U1.Y10 (IO_L8N_HDGC_85)
- net HDMI_DR0: now also U1.W9 (IO_L11P_AD9P_85); no longer U1.AC12 (IO_L1P_AD15P_85)
- net HDMI_DR1: now also U1.W8 (IO_L11N_AD9N_85); no longer U1.AC11 (IO_L1N_AD15N_85)
- net HDMI_DR2: now also U1.AA8 (IO_L9N_AD11N_85); no longer U1.AD11 (IO_L2P_AD14P_85)
- net HDMI_DR3: now also U1.Y8 (IO_L9P_AD11P_85); no longer U1.AE11 (IO_L2N_AD14N_85)
- net HDMI_DR4: now also U1.W10 (IO_L12N_AD8N_85); no longer U1.AC9 (IO_L3P_AD13P_85)
- net HDMI_DR5: now also U1.W11 (IO_L12P_AD8P_85); no longer U1.AD9 (IO_L3N_AD13N_85)
- net HDMI_DR6: now also U1.V11 (IO_L10N_AD10N_85); no longer U1.AE10 (IO_L4P_AD12P_85)
- net HDMI_DR7: now also U1.V12 (IO_L10P_AD10P_85); no longer U1.AF10 (IO_L4N_AD12N_85)
- net HDMI_HSYNC: now also U1.AB15 (IO_L7N_HDGC_AD5N_84); no longer U1.W15 (IO_L8P_HDGC_AD4P_84)
- net HDMI_IDCLK: now also U1.W15 (IO_L8P_HDGC_AD4P_84); no longer U1.AA15 (IO_L7P_HDGC_AD5P_84)
- net HDMI_INT: now also U1.AE12 (IO_L4P_AD8P_84); no longer U1.AD14 (IO_L6P_HDGC_AD6P_84)
- net HDMI_MCLK: now also U1.AF13 (IO_L2N_AD10N_84); no longer U1.AC13 (IO_L5N_HDGC_AD7N_84)
- net HDMI_RST: now also U1.AF12 (IO_L4N_AD8N_84); no longer U1.AD13 (IO_L6N_HDGC_AD6N_84)
- net HDMI_SCK: now also U1.AD13 (IO_L6N_HDGC_AD6N_84); no longer U1.AC14 (IO_L5P_HDGC_AD7P_84)
- net HDMI_SD0_DL0: now also U1.AE15 (IO_L3N_AD9N_84); no longer U1.AE12 (IO_L4P_AD8P_84)
- net HDMI_SD1_DR1: now also U1.AD15 (IO_L3P_AD9P_84); no longer U1.AE15 (IO_L3N_AD9N_84)
- net HDMI_SD2_DL1: now also U1.AD14 (IO_L6P_HDGC_AD6P_84); no longer U1.AD15 (IO_L3P_AD9P_84)
- net HDMI_SD3_DR2: now also U1.AC14 (IO_L5P_HDGC_AD7P_84); no longer U1.AF13 (IO_L2N_AD10N_84)
- net HDMI_SPDIF: now also U1.AC13 (IO_L5N_HDGC_AD7N_84); no longer U1.AF14 (IO_L2P_AD10P_84)
- net HDMI_VSYNC: now also U1.Y15 (IO_L8N_HDGC_AD4N_84); no longer U1.AB15 (IO_L7N_HDGC_AD5N_84)
- net HDMI_WS_DR0: now also U1.AF14 (IO_L2P_AD10P_84); no longer U1.AF12 (IO_L4N_AD8N_84)
- net MBUS_D0: now also U1.G12 (IO_L11P_T1U_N8_GC_66); no longer U1.E11 (IO_L14P_T2L_N2_GC_66)
- net MBUS_D1: now also U1.H12 (IO_T3U_N12_66); no longer U1.D11 (IO_L14N_T2L_N3_GC_66)
- net MBUS_D10: now also U1.F15 (IO_L8N_T1L_N3_AD5N_66); no longer U1.D9 (IO_T2U_N12_66)
- net MBUS_D11: now also U1.G15 (IO_L8P_T1L_N2_AD5P_66); no longer U1.H12 (IO_T3U_N12_66)
- net MBUS_D2: now also U1.A13 (IO_L6P_T0U_N10_AD6P_66); no longer U1.C9 (IO_L15P_T2L_N4_AD11P_66)
- net MBUS_D3: now also U1.H13 (IO_L9N_T1L_N5_AD12N_66); no longer U1.C8 (IO_L15N_T2L_N5_AD11N_66)
- net MBUS_D4: now also U1.J13 (IO_L9P_T1L_N4_AD12P_66); no longer U1.C11 (IO_L16P_T2U_N6_QBC_AD3P_66)
- net MBUS_D5: now also U1.C14 (IO_L1N_T0L_N1_DBC_66); no longer U1.B11 (IO_L16N_T2U_N7_QBC_AD3N_66)
- net MBUS_D6: now also U1.D14 (IO_L1P_T0L_N0_DBC_66); no longer U1.E8 (IO_L17P_T2U_N8_AD10P_66)
- net MBUS_D7: now also U1.F14 (IO_L10P_T1U_N6_QBC_AD4P_66); no longer U1.D8 (IO_L17N_T2U_N9_AD10N_66)
- net MBUS_D8: now also U1.G14 (IO_L7N_T1L_N1_QBC_AD13N_66); no longer U1.B10 (IO_L18P_T2U_N10_AD2P_66)
- net MBUS_D9: now also U1.H14 (IO_L7P_T1L_N0_QBC_AD13P_66); no longer U1.A10 (IO_L18N_T2U_N11_AD2N_66)
- net MIPI_D0_N: now also U1.Y20 (IO_L12N_T1U_N11_GC_A09_D25_65); no longer U1.AB20 (IO_L14N_T2L_N3_GC_A05_D21_65)
- net MIPI_D0_P: now also U1.W20 (IO_L12P_T1U_N10_GC_A08_D24_65); no longer U1.AB19 (IO_L14P_T2L_N2_GC_A04_D20_65)
- net RST0: now also U1.A22 (IO_L7P_T1L_N0_QBC_AD13P_67); no longer U1.C17 (IO_L18P_T2U_N10_AD2P_67)
- net RST1: now also U1.B17 (IO_L18N_T2U_N11_AD2N_67); no longer U1.D23 (IO_L4P_T0U_N6_DBC_AD7P_67)
- net RST2: now also U1.R23 (IO_L16N_T2U_N7_QBC_AD3N_64); no longer U1.AB22 (IO_L3N_T0L_N5_AD15N_64)
- net RST3: now also U1.U24 (IO_L11P_T1U_N8_GC_64); no longer U1.U26 (IO_L10P_T1U_N6_QBC_AD4P_64)
- net RWDS0_0: now also U1.B20 (IO_L8P_T1L_N2_AD5P_67); no longer U1.F17 (IO_L20N_T3L_N3_AD1N_67)
- net RWDS0_1: now also U1.C26 (IO_L6P_T0U_N10_AD6P_67); no longer U1.C19 (IO_L13N_T2L_N1_GC_QBC_67)
- net RWDS1_0: now also U1.B16 (IO_L17N_T2U_N9_AD10N_67); no longer U1.B20 (IO_L8P_T1L_N2_AD5P_67)
- net RWDS1_1: now also U1.F18 (IO_L21P_T3L_N4_AD8P_67); no longer U1.B26 (IO_L6N_T0U_N11_AD6N_67)
- net RWDS2_0: now also U1.T22 (IO_L14P_T2L_N2_GC_64); no longer U1.U25 (IO_T1U_N12_64)
- net RWDS2_1: now also U1.R25 (IO_L18N_T2U_N11_AD2N_64); no longer U1.W23 (IO_L7P_T1L_N0_QBC_AD13P_64)
- net RWDS3_0: now also U1.Y23 (IO_L5P_T0U_N8_AD14P_64); no longer U1.P26 (IO_L15P_T2L_N4_AD11P_64)
- net RWDS3_1: now also U1.AC23 (IO_L6P_T0U_N10_AD6P_64); no longer U1.R26 (IO_L15N_T2L_N5_AD11N_64)
- net SYSCLK0_N: now also U1.C19 (IO_L13N_T2L_N1_GC_QBC_67); no longer U1.D21 (IO_L12N_T1U_N11_GC_67)
- net SYSCLK0_P: now also U1.D19 (IO_L13P_T2L_N0_GC_QBC_67); no longer U1.D20 (IO_L12P_T1U_N10_GC_67)
- no-connect marks 101 -> 92
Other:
- note added: "1V8 HyperRam 0/1"
- note added: "1V8 HyperRam 2/3"
- note removed: "1V8 HyperRam"
- moved on the sheet: R3

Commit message: Rev 2 PCB's and Heatsink PCB's complete
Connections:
- net CAM_LED_EN: now also U1.Y11 (IO_L8P_HDGC_85); no longer U1.AB14 (IO_L9N_AD3N_84)
- net CAM_PWR_EN: now also U1.Y10 (IO_L8N_HDGC_85); no longer U1.AA14 (IO_L9P_AD3P_84)
- net HDMI_DG0: now also U1.AD14 (IO_L6P_HDGC_AD6P_84); no longer U1.Y11 (IO_L8P_HDGC_85)
- net HDMI_DG1: now also U1.AD13 (IO_L6N_HDGC_AD6N_84); no longer U1.Y10 (IO_L8N_HDGC_85)
- net HDMI_DG2: now also U1.AC14 (IO_L5P_HDGC_AD7P_84); no longer U1.AA10 (IO_L7P_HDGC_85)
- net HDMI_DG3: now also U1.AC13 (IO_L5N_HDGC_AD7N_84); no longer U1.AB10 (IO_L6P_HDGC_85)
- net HDMI_DG4: now also U1.AB12 (IO_L12P_AD0P_84); no longer U1.AA9 (IO_L7N_HDGC_85)
- net HDMI_DG5: now also U1.AB11 (IO_L12N_AD0N_84); no longer U1.AB9 (IO_L6N_HDGC_85)
- net HDMI_DR0: now also U1.AB10 (IO_L6P_HDGC_85); no longer U1.W9 (IO_L11P_AD9P_85)
- net HDMI_DR1: now also U1.AB9 (IO_L6N_HDGC_85); no longer U1.W8 (IO_L11N_AD9N_85)
- net HDMI_DR2: now also U1.AA10 (IO_L7P_HDGC_85); no longer U1.AA8 (IO_L9N_AD11N_85)
- net HDMI_DR3: now also U1.AA9 (IO_L7N_HDGC_85); no longer U1.Y8 (IO_L9P_AD11P_85)
- net HDMI_DR4: now also U1.AA8 (IO_L9N_AD11N_85); no longer U1.W10 (IO_L12N_AD8N_85)
- net HDMI_DR5: now also U1.W9 (IO_L11P_AD9P_85); no longer U1.W11 (IO_L12P_AD8P_85)
- net HDMI_DR6: now also U1.Y8 (IO_L9P_AD11P_85); no longer U1.V11 (IO_L10N_AD10N_85)
- net HDMI_DR7: now also U1.W8 (IO_L11N_AD9N_85); no longer U1.V12 (IO_L10P_AD10P_85)
- net HDMI_SCK: now also U1.AA12 (IO_L11N_AD1N_84); no longer U1.AD13 (IO_L6N_HDGC_AD6N_84)
- net HDMI_SD2_DL1: now also U1.AA13 (IO_L11P_AD1P_84); no longer U1.AD14 (IO_L6P_HDGC_AD6P_84)
- net HDMI_SD3_DR2: now also U1.V11 (IO_L10N_AD10N_85); no longer U1.AC14 (IO_L5P_HDGC_AD7P_84)
- net HDMI_SPDIF: now also U1.V12 (IO_L10P_AD10P_85); no longer U1.AC13 (IO_L5N_HDGC_AD7N_84)
- net IO0: now also U1.F8 (IO_L20N_T3L_N3_AD1N_66); no longer U1.J9 (IO_L21N_T3L_N5_AD8N_66)
- net IO1: now also U1.H8 (IO_L19N_T3L_N1_DBC_AD9N_66); no longer U1.F8 (IO_L20N_T3L_N3_AD1N_66)
- net IO2: now also U1.F9 (IO_L20P_T3L_N2_AD1P_66); no longer U1.H9 (IO_L19P_T3L_N0_DBC_AD9P_66)
- net IO3: now also U1.G9 (IO_L24N_T3U_N11_66); no longer U1.H8 (IO_L19N_T3L_N1_DBC_AD9N_66)
- net IO4: now also U1.H9 (IO_L19P_T3L_N0_DBC_AD9P_66); no longer U1.G11 (IO_L22P_T3U_N6_DBC_AD0P_66)
- net IO5: now also U1.J9 (IO_L21N_T3L_N5_AD8N_66); no longer U1.F10 (IO_L22N_T3U_N7_DBC_AD0N_66)
- net IO6: now also U1.F10 (IO_L22N_T3U_N7_DBC_AD0N_66); no longer U1.F9 (IO_L20P_T3L_N2_AD1P_66)
- net IO7: now also U1.G10 (IO_L24P_T3U_N10_66); no longer U1.J10 (IO_L21P_T3L_N4_AD8P_66)
- net LED0: now also U1.H11 (IO_L23N_T3U_N9_66); no longer U1.J11 (IO_L23P_T3U_N8_66)
- net LED1: now also U1.J11 (IO_L23P_T3U_N8_66); no longer U1.H11 (IO_L23N_T3U_N9_66)
- net LED2: now also U1.J10 (IO_L21P_T3L_N4_AD8P_66); no longer U1.G10 (IO_L24P_T3U_N10_66)
- net LED3: now also U1.G11 (IO_L22P_T3U_N6_DBC_AD0P_66); no longer U1.G9 (IO_L24N_T3U_N11_66)
- net SYS_SPI_CS: now also U1.W14 (IO_L10P_AD2P_84); no longer U1.W13 (IO_L10N_AD2N_84)
- net SYS_SPI_MISO: now also U1.W13 (IO_L10N_AD2N_84); no longer U1.W14 (IO_L10P_AD2P_84)
- net SYS_SPI_MOSI: now also U1.AA14 (IO_L9P_AD3P_84); no longer U1.AA12 (IO_L11N_AD1N_84)
- net SYS_SPI_SCK: now also U1.AB14 (IO_L9N_AD3N_84); no longer U1.AA13 (IO_L11P_AD1P_84)
- net UART_RX: now also U1.W10 (IO_L12N_AD8N_85); no longer U1.AB11 (IO_L12N_AD0N_84)
- net UART_TX: now also U1.W11 (IO_L12P_AD8P_85); no longer U1.AB12 (IO_L12P_AD0P_84)
- no-connect marks 92 -> 103

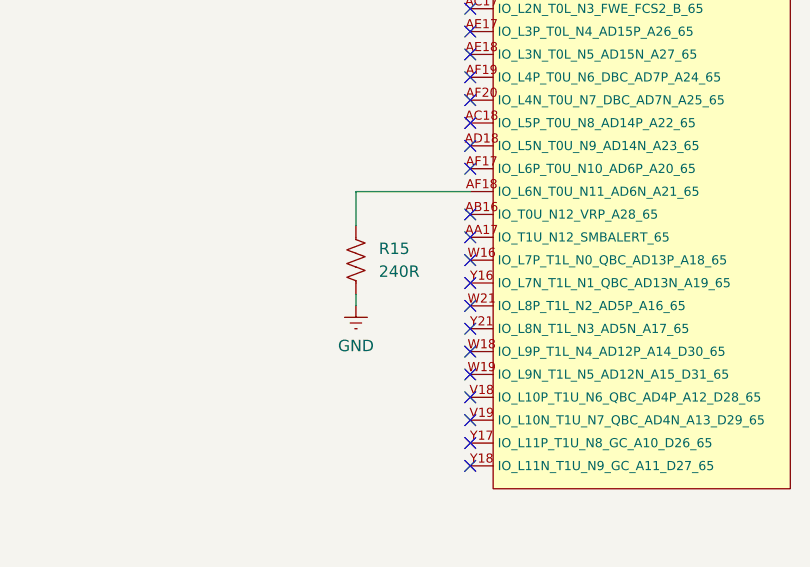
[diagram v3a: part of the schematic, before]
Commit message: Updated Schematics & created pixel combiner HDL
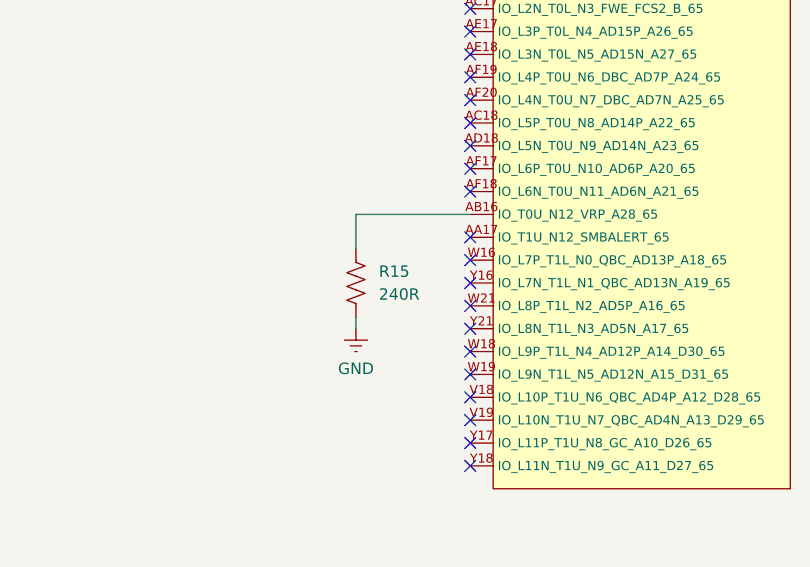
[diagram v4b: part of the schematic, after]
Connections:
- net at U1.AB16 (IO_T0U_N12_VRP_A28_65): now also R15.2
- net at U1.AF18 (IO_L6N_T0U_N11_AD6N_A21_65): no longer R15.2
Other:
- moved on the sheet: R15
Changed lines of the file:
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@@
 	)
 	(no_connect
+		(at 529.59 322.58)
+	)
+	(no_connect
 		(at 438.15 109.22)
 	)
@@
 	)
 	(no_connect
-		(at 529.59 325.12)
-	)
-	(no_connect
 		(at 438.15 154.94)
 	)
@@
 	(wire
 		(pts
-			(xy 516.89 322.58) (xy 516.89 326.39)
-		)
-		(stroke
-			(width 0)
-			(type default)
-		)
-	)
-	(wire
-		(pts
 			(xy 242.57 83.82) (xy 242.57 86.36)
 		)
@@
 	(wire
 		(pts
-			(xy 516.89 334.01) (xy 516.89 335.28)
+			(xy 516.89 336.55) (xy 516.89 337.82)
 		)
 		(stroke
@@
 	(wire
 		(pts
+			(xy 516.89 325.12) (xy 516.89 328.93)
+		)
+		(stroke
+			(width 0)
+			(type default)
+		)
+	)
+	(wire
+		(pts
 			(xy 514.35 161.29) (xy 529.59 161.29)
 		)
@@
 		)
 	)
+	(wire
+		(pts
+			(xy 516.89 325.12) (xy 529.59 325.12)
+		)
+		(stroke
+			(width 0)
+			(type default)
+		)
+	)
 	(bus
 		(pts
@@
 	(wire
 		(pts
-			(xy 529.59 322.58) (xy 516.89 322.58)
-		)
-		(stroke
-			(width 0)
-			(type default)
-		)
-	)
-	(wire
-		(pts
 			(xy 375.92 81.28) (xy 379.73 81.28)
 		)
@@
 	(symbol
 		(lib_id "power:GND")
-		(at 516.89 335.28 0)
+		(at 516.89 337.82 0)
 		(unit 1)
 		(exclude_from_sim no)
@@
 		(dnp no)
 		(property "Reference" "#PWR030"
-			(at 516.89 341.63 0)
+			(at 516.89 344.17 0)
 			(effects
 				(font
@@
 		)
 		(property "Value" "GND"
-			(at 516.89 339.725 0)
+			(at 516.89 342.265 0)
 			(effects
 				(font
@@
 		)
 		(property "Footprint" ""
-			(at 516.89 335.28 0)
+			(at 516.89 337.82 0)
 			(effects
 				(font
@@
 		)
 		(property "Datasheet" ""
-			(at 516.89 335.28 0)
+			(at 516.89 337.82 0)
 			(effects
 				(font
@@
 		)
 		(property "Description" "Power symbol creates a global label with name \"GND\" , ground"
-			(at 516.89 335.28 0)
+			(at 516.89 337.82 0)
 			(effects
 				(font
@@
 	(symbol
 		(lib_id "Device:R_US")
-		(at 516.89 330.2 180)
+		(at 516.89 332.74 180)
 		(unit 1)
 		(exclude_from_sim no)
@@
 		(fields_autoplaced yes)
 		(property "Reference" "R15"
-			(at 519.43 328.9299 0)
+			(at 519.43 331.4699 0)
 			(effects
 				(font
@@
 		)
 		(property "Value" "240R"
-			(at 519.43 331.4699 0)
+			(at 519.43 334.0099 0)
 			(effects
 				(font
@@
 		)
 		(property "Footprint" "Resistor_SMD:R_0201_0603Metric"
-			(at 515.874 329.946 90)
+			(at 515.874 332.486 90)
 			(effects
 				(font
@@
 		)
 		(property "Datasheet" "~"
-			(at 516.89 330.2 0)
+			(at 516.89 332.74 0)
 			(effects
 				(font
@@
 		)
 		(property "Description" "Resistor, US symbol"
-			(at 516.89 330.2 0)
+			(at 516.89 332.74 0)
 			(effects
 				(font

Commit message: Added Presentation Slides
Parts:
- R15: now not fitted
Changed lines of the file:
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@@
 		(in_bom yes)
 		(on_board yes)
-		(dnp no)
+		(dnp yes)
 		(fields_autoplaced yes)
 		(property "Reference" "R15"
